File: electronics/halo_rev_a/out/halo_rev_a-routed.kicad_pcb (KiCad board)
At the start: 4 copper layers, 25.6 x 26 mm, 62 parts, among them J1 TC2030, J2 UWB stub, U1 nRF54L10-QFAA-R7, U2 LIS2DW12TR, X1 32.768kHz, X2 32MHz

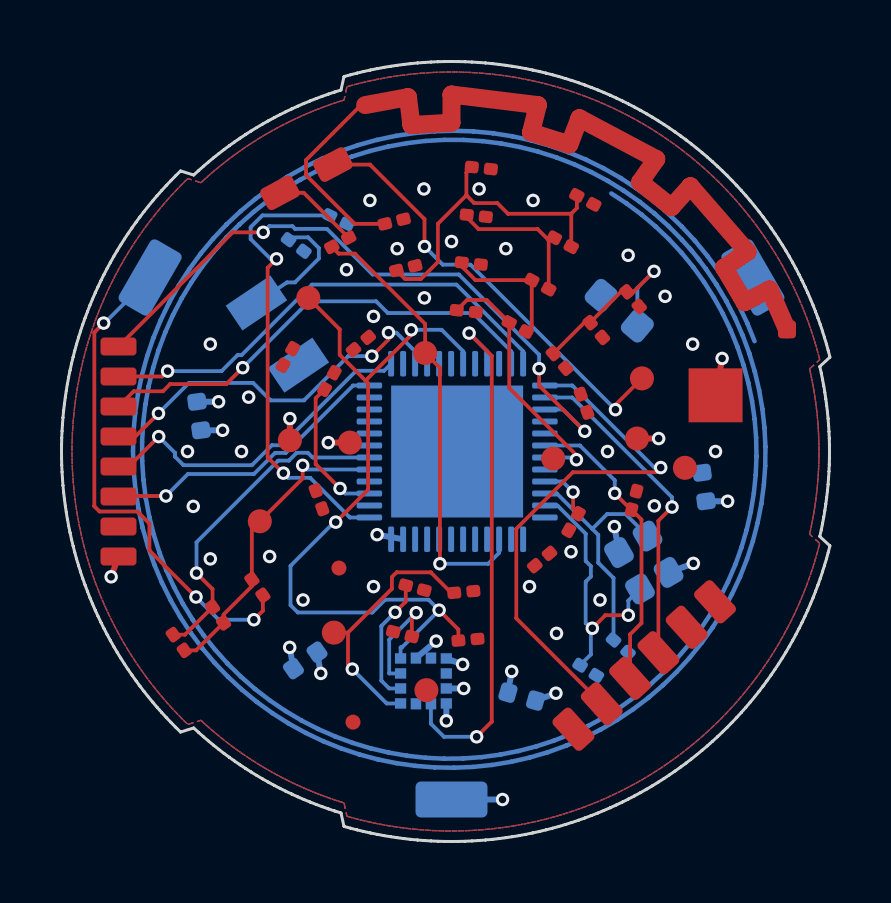
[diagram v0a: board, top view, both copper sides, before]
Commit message: B1: routed on the corrected geometry — 81 -> 33 unconnected, 0 errors, arm clear
Second route, on the nine-tooth board with the antenna-arm-shadow keep-out.

                        4-tooth run    9-tooth run
    unconnected          81 -> 35       81 -> 33
    DRC errors            0 -> 0         0 -> 0
    DRC warnings          3 -> 2         3 -> 3
    segments            255 -> 553     275 -> 649
    vias                 49 -> 86       49 -> 91
    wall time             ~857 s         464.8 s
    worst protected disp    55 nm          55 nm
    conductor          162.2257 ->    162.2479 ->
                       162.2258 mm    162.2480 mm
    arm clearance      -0.1747 mm     +0.3627 mm

check_routed: 9 PASS / 0 FAIL / 0 CANNOT DETERMINE.

THE KEEP-OUT HELD. The router put nothing under the arm: clearance on the
routed board is 0.3627 mm, identical to the unrouted board, so the 46 % faster
route is not a route that took shortcuts through the antenna. Fiducial keep-outs
cost nothing this time — 0 DRC errors again, and unconnected went 35 -> 33
rather than the other way, so the trade is strictly better at nine teeth.

TWO DEFECTS IN THIS CHECK, BOTH FOUND BY ITS OWN NEGATIVE CONTROL.

1. R9 GRADED THE WHOLE NET AS THE RADIATOR. ANT_FEED also carries the run from
   L10 out to the element's tap, which the router draws at the netclass width.
   Measured: 37 segments at 0.600 mm forming the radiator, 2 at 0.127 mm
   running out to the feed. R9 reported the coil 0.0262 mm from "the arm" when
   what it was near was that feed run — a false FAIL on a good board. ce-rf's
   own model draws the same line: "the feed tap and any copper past the short
   are NOT in" the resonant arm. R9 now grades only copper at the element's own
   width and reports the split every run.

2. A SEGMENT THE PARSER COULD NOT READ VANISHED SILENTLY. `(net "GND")` is what
   KiCad 10 writes, but `(net 2 "GND")` and a bare `(net 2)` are both legal. The
   net regex matched only the first, and the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
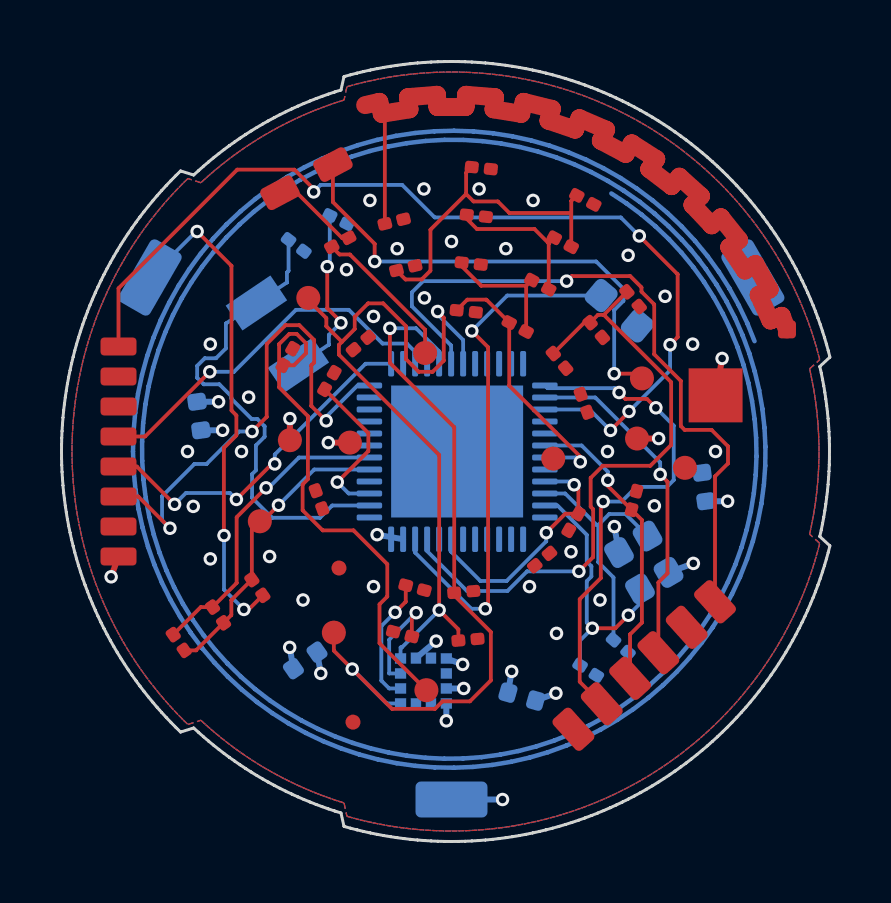
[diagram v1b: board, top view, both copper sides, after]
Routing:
- net SWO: track 0.00 -> 23.3 mm, vias 0 -> 1
- net DCC: track 0.00 -> 17.9 mm, vias 0 -> 2
- net ACC_INT2: track 17.6 -> 0.00 mm, vias 2 -> 0
- net NFC2: track 67.8 -> 84.8 mm
- net UWB_IRQ: track 16.1 -> 0.00 mm, vias 1 -> 0
- net I2C_SCL: track 8.71 -> 24.6 mm, vias 1 -> 2
- net UWB_CS: track 15.6 -> 0.00 mm, vias 1 -> 0
- net DECD: track 6.54 -> 21.3 mm
- net XL2: track 4.16 -> 16.2 mm
- net UWB_RST: track 22.3 -> 32.5 mm, vias 3 -> 5
- net PIEZO_P: track 15.0 -> 5.03 mm, vias 1 -> 0
- net XL1: track 15.3 -> 5.92 mm
- net SPI_SCK: track 9.90 -> 17.3 mm, vias 1 -> 3
- net DECA: track 1.88 -> 8.20 mm, vias 1 -> 2
- net ANT_FEED: track 31.0 -> 28.2 mm
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
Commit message: B1: routed with the planes cleared — 83 -> 28 unconnected, ROUTE GATE PASS
Third route, on the geometry with nfc-coil-clearance cutting the planes out
from under the coil. First run of this lane where check_routed returns a clean
sweep.

                      4-tooth      9-tooth      9-tooth + planes cleared
  unconnected         81 -> 35     81 -> 33     83 -> 28
  DRC errors           0 -> 0       0 -> 0       0 -> 0
  DRC warnings         3 -> 2       3 -> 3       3 -> 3
  segments           255 -> 553   275 -> 649   275 -> 610
  vias                49 -> 86     49 -> 91     49 -> 83
  wall time             857 s        465 s       1155 s
  worst protected      55 nm        55 nm        55 nm
  conductor        162.2257 ->  162.2479 ->  162.2479 ->
                   162.2258 mm  162.2480 mm  162.2480 mm
  arm clearance     -0.1747 mm   +0.3627 mm   +0.3627 mm
  check_routed      5P/2F        9P/0F        9 PASS / 0 FAIL / 0 CD

THE TWO CONNECTIONS THE PLANE CUT COST WERE PAID BACK WITH INTEREST. Clearing
the planes took the unrouted board 81 -> 83; the routed board came back at 28,
five better than the 33 of the previous geometry and seven better than the 35
of the first. The pour was not carrying those nets usefully — it was in the
way, and the router found better paths once it was gone. The cost was real and
so is the return, and both are measured rather than argued.

It cost time: 1155 s against 465 s, because the copper the router had been
leaning on is no longer there. That is the trade and it is worth it.

Protected copper untouched again: all 255 segments of the antenna and the coil
back within 55 nm of where they were sent, under the 100 nm the interchange
format carries; conductor 162.2479 -> 162.2480 mm. The 34 segments added on
those nets are the router reaching their pads. Arm clearance 0.3627 mm,
identical to the unrouted board — the keep-outs held on all three runs.

Co-Authored-By: Claude Opus 5 (1M context) <noreply@anthropic.com>
Claude-Session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
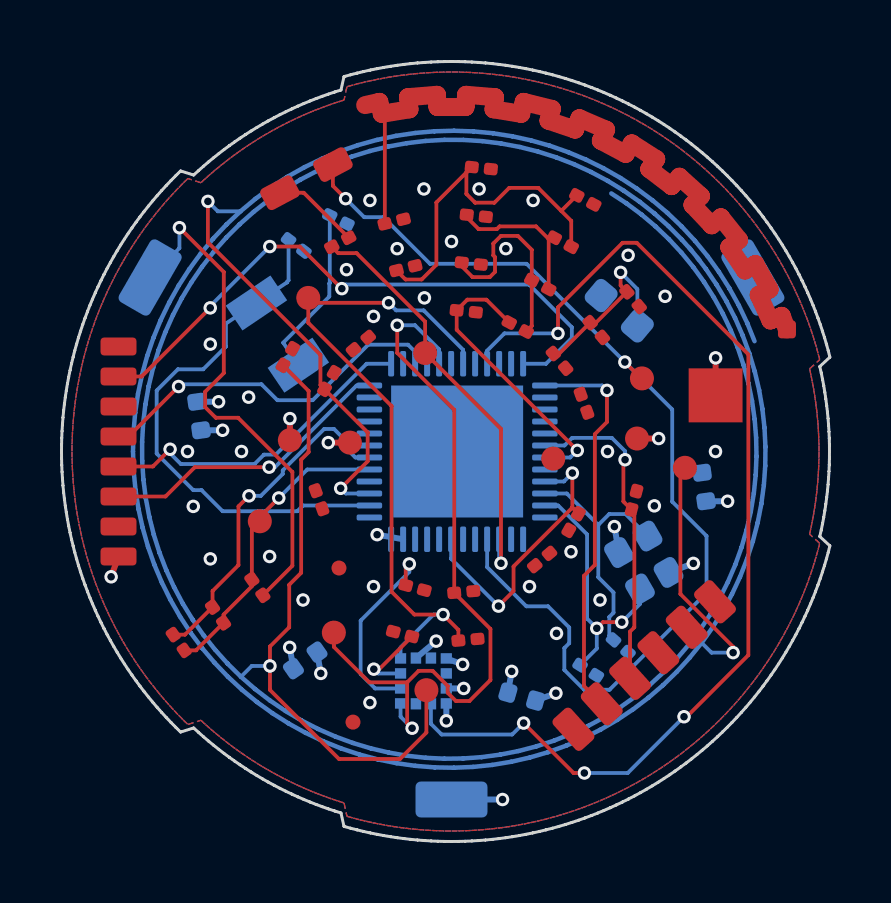
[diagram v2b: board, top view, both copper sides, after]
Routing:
- net ACC_INT2: track 0.00 -> 36.6 mm, vias 0 -> 4
- net UWB_RST: track 32.5 -> 0.00 mm, vias 5 -> 0
- net SWO: track 23.3 -> 0.00 mm, vias 1 -> 0
- net UWB_IRQ: track 0.00 -> 20.5 mm, vias 0 -> 3
- net PIEZO_N: track 16.4 -> 34.8 mm
- net DCC: track 17.9 -> 0.00 mm, vias 2 -> 0
- net NFC1: track 75.3 -> 92.5 mm, vias 1 -> 3
- net DECD: track 21.3 -> 6.06 mm
- net SWDCLK: track 11.3 -> 0.00 mm, vias 1 -> 0
- net PIEZO_P: track 5.03 -> 14.1 mm, vias 0 -> 1
- net SPI_SCK: track 17.3 -> 9.90 mm, vias 3 -> 1
- net NFC2: track 84.8 -> 88.6 mm, vias 0 -> 1
- net SWDIO: track 16.7 -> 13.1 mm, vias 3 -> 1
- net I2C_SDA: track 25.5 -> 22.6 mm
- net RF_A: track 4.33 -> 6.80 mm
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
